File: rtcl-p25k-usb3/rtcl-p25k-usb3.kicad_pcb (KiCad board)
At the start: 2 copper layers, 83 parts, among them J5 JTAG, U1 FT601Q, U12 TPS22917DBV, U2 TPD4E05U06DQA, U3 USBLC6-2P6

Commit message: WIP
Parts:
- added R51: 0, Resistor_SMD:R_0402_1005Metric, F.Cu at (159.3, 102.0)
- added R52: 0, Resistor_SMD:R_0402_1005Metric, F.Cu at (159.3, 103.0)
- added RN1: R_Pack04, Resistor_SMD:R_Array_Convex_4x0603, F.Cu at (156.6, 103.6)
- added Y1: 30MHz, Resistor_SMD:R_Array_Convex_4x0402, F.Cu at (169.9, 103.7)
- L1: footprint Inductor_SMD:L_0603_1608Metric -> Resistor_SMD:R_0402_1005Metric
- R1, R10, R11, R12, R13, R14, R15, R16, R17, R18, R19, R2, R20, R21, R22, R23, R24, R25, R26, R27, R28, R29, R3, R30, R31, R32, R33, R34, R35, R36, R37, R38, R39, R4, R40, R41, R42, R43, R44, R45, R46, R47, R48, R49, R5, R50, R51, R52, R53, R54, R55, R56, R57, R58, R6, R7, R8, R9: footprint Resistor_SMD:R_0603_1608Metric -> Resistor_SMD:R_0402_1005Metric
- moved R51 24.2 mm to (159.3, 104.0)
- moved R52 23.8 mm to (159.3, 105.0)
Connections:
- R39 pad 1: /FT601_BE0 -> unconnected-(R39-Pad1)
- R40 pad 1: /FT601_BE1 -> unconnected-(R40-Pad1)
- R41 pad 1: /FT601_BE2 -> unconnected-(R41-Pad1)
- R42 pad 1: /FT601_BE3 -> unconnected-(R42-Pad1)

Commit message: WIP
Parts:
- added J3: BTB-DF40C-60DS-0.4V(51), rtcl-p25k-usb3:CONN_DF40C-60DS_HIR, F.Cu at (150.0, 107.0)
- added J4: BTB-DF40C-60DS-0.4V(51), rtcl-p25k-usb3:CONN_DF40C-60DS_HIR, F.Cu at (150.0, 93.0)
- moved C13 100.7 mm to (46.0, 148.6)
- moved C14 100.7 mm to (46.0, 151.1)
- moved C5 100.7 mm to (46.0, 141.1)
- moved C69 100.7 mm to (74.9, 155.8)
- moved D1 100.7 mm to (45.6, 171.1)
- moved J5 100.7 mm to (70.4, 142.1)
- moved L1 100.7 mm to (46.0, 158.7)
- moved R12 100.7 mm to (50.0, 158.7)
- moved R15 100.7 mm to (50.0, 166.2)
- moved R17 100.7 mm to (54.0, 141.1)
- moved R20 100.7 mm to (54.0, 148.6)
- moved R21 100.7 mm to (54.0, 151.1)
- moved R24 100.7 mm to (54.0, 158.7)
- moved R27 100.7 mm to (54.0, 166.2)
- moved R29 100.7 mm to (58.1, 141.1)
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- renumbered Y1 to X1

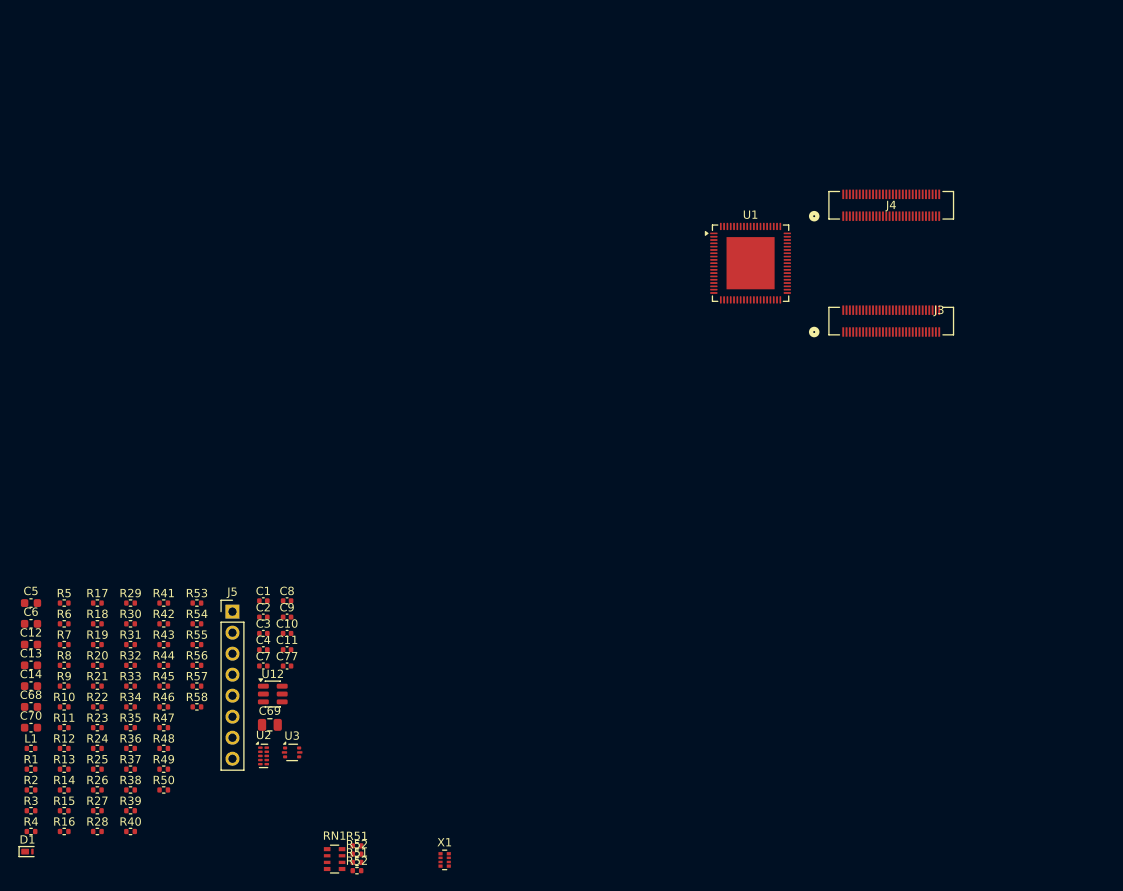
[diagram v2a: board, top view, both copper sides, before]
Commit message: Add new footprints for RES_YC104_YAG and RES_YC164_3P2X1P6_YAG
- Created footprint for RES_YC104_YAG with detailed properties and pads.
- Created footprint for RES_YC164_3P2X1P6_YAG with comprehensive design elements and specifications.
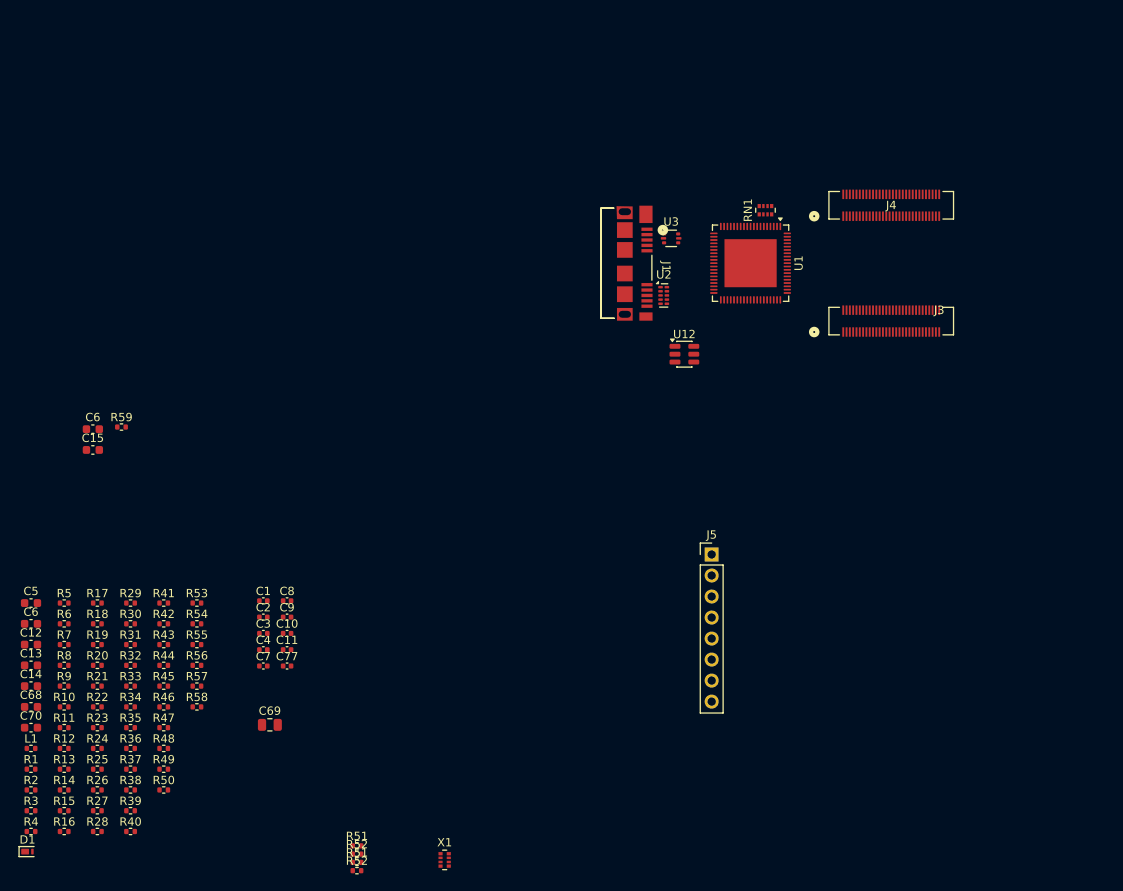
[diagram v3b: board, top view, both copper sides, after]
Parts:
- added C15: 0.1uF, Capacitor_SMD:C_0603_1608Metric, F.Cu at (53.5, 122.6)
- added C6: 4.7uF, Capacitor_SMD:C_0603_1608Metric, F.Cu at (53.5, 120.1)
- added J1: ZX360D-B-10P(30), rtcl-p25k-usb3:CONN10_ZX360D-B-10P30_HIR, F.Cu at (118.0, 100.0)
- added R59: 1M, Resistor_SMD:R_0402_1005Metric, F.Cu at (57.0, 119.8)
- RN1: footprint Resistor_SMD:R_Array_Convex_4x0603 -> Resistor_SMD:R_Array_Convex_4x0402
- moved RN1 94.1 mm to (134.8, 93.6), turned to 90 degrees
- moved U3 77.2 mm to (123.4, 97.0)
- moved U2 73.7 mm to (122.5, 103.9)
- moved U12 64.5 mm to (125.0, 111.0)
- moved J5 58.3 mm to (128.3, 135.2)
- turned U1 to -90 degrees
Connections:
- C10 pad 2: +5V -> VBUS
- RN1 pad 1: unconnected-(RN1-R1.1-Pad1) -> /FT601_BE3
- RN1 pad 2: unconnected-(RN1-R2.1-Pad2) -> /FT601_BE2
- RN1 pad 3: unconnected-(RN1-R3.1-Pad3) -> /FT601_BE1
- RN1 pad 4: unconnected-(RN1-R4.1-Pad4) -> /FT601_BE0
- RN1 pad 5: /FT601_BE0 -> unconnected-(RN1-R4.2-Pad5)
- RN1 pad 6: /FT601_BE1 -> unconnected-(RN1-R3.2-Pad6)
- RN1 pad 7: /FT601_BE2 -> unconnected-(RN1-R2.2-Pad7)
- RN1 pad 8: /FT601_BE3 -> unconnected-(RN1-R1.2-Pad8)
- U1 pad 37: +5V -> VBUS
- U2 pad 1: /USB_SSRXP -> /USB_SSTXM
- U2 pad 2: /USB_SSRXM -> /USB_SSTXP
- U2 pad 4: /USB_SSTXP -> /USB_SSRXM
- U2 pad 5: /USB_SSTXM -> /USB_SSRXP
- U3 pad 5: +5V -> VBUS

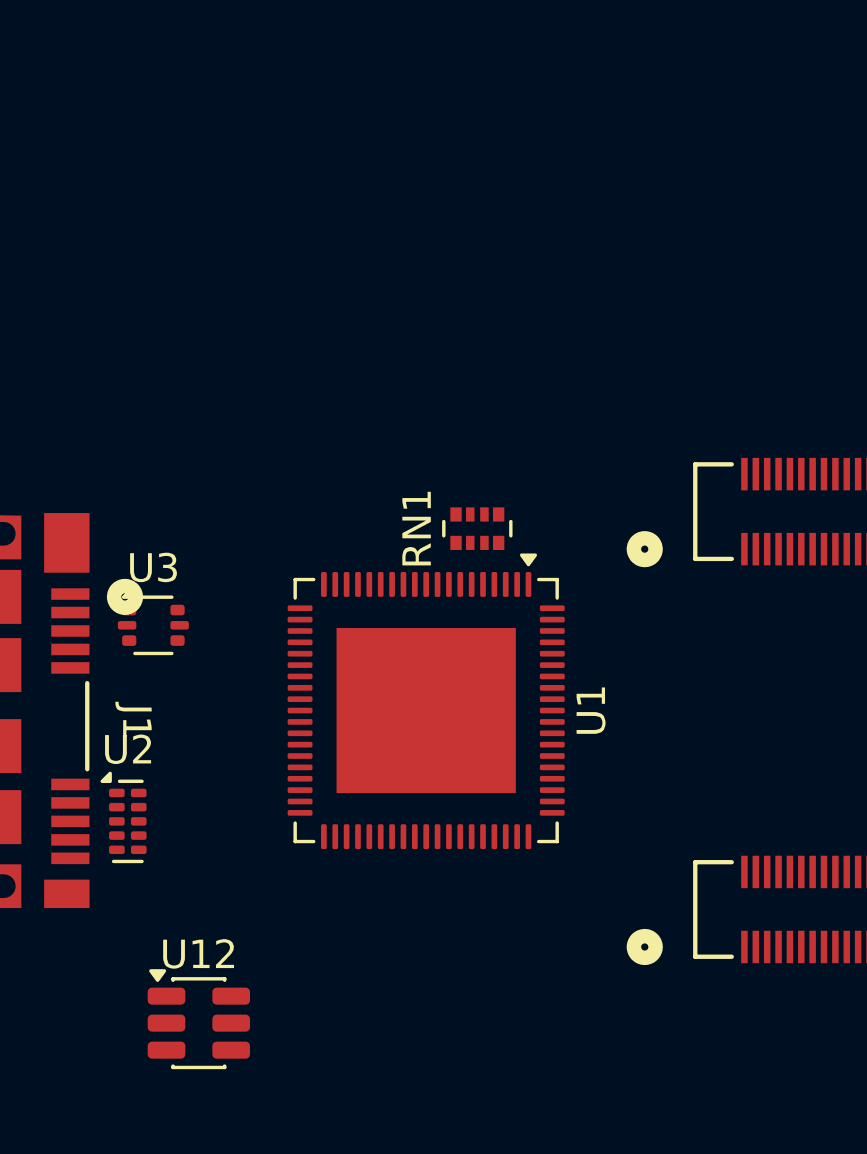
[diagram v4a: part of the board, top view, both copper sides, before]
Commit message: Add FT601Q symbol to KiCad library
- Created a new symbol for the FT601Q USB 3.0 FIFO interface IC.
- Included properties such as Reference, Value, Footprint, Datasheet, and Description.
- Defined 77 pins with appropriate names, types, and attributes.
- Ensured compatibility with KiCad version 10.0 and included necessary font settings.
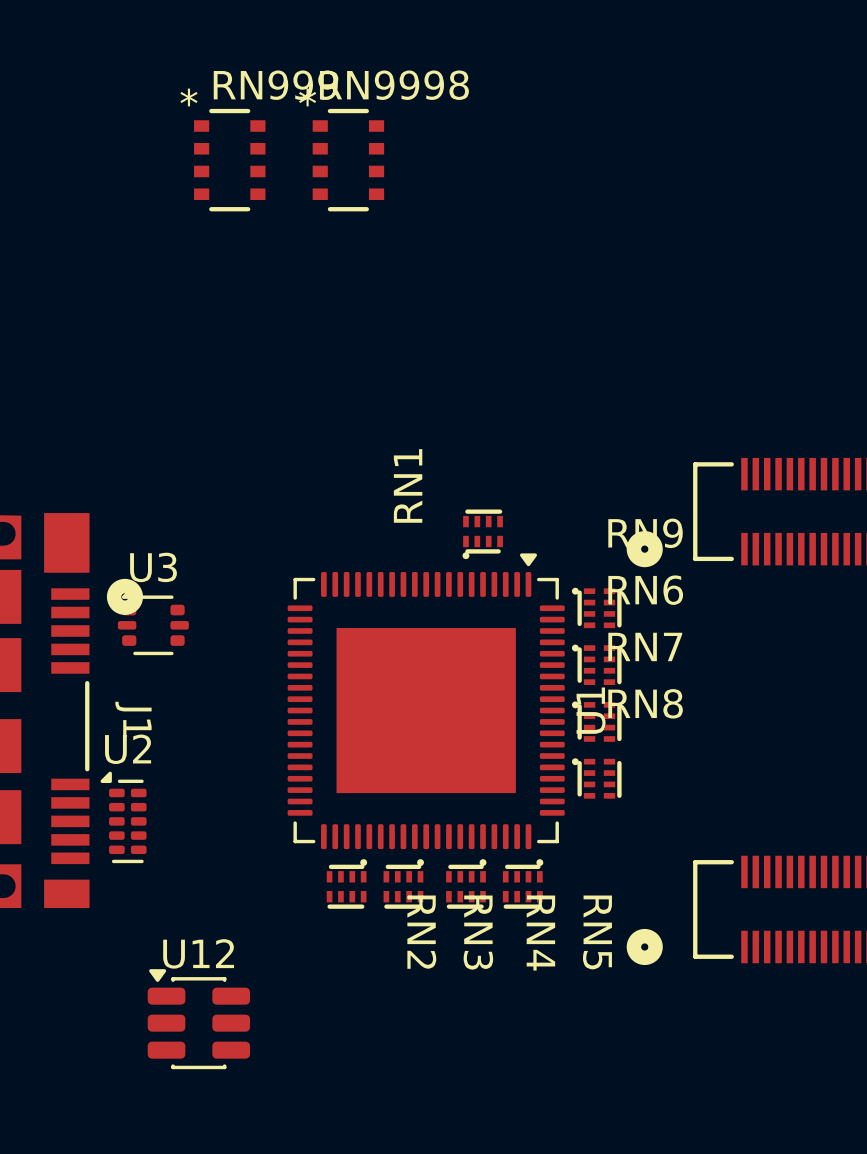
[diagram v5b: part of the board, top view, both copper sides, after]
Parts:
- added RN2: YC104-JR-0722RL, rtcl-p25k-usb3:RES_YC104_YAG, F.Cu at (130.2, 106.2)
- added RN3: YC104-JR-0722RL, rtcl-p25k-usb3:RES_YC104_YAG, F.Cu at (132.2, 106.2)
- added RN4: YC104-JR-0722RL, rtcl-p25k-usb3:RES_YC104_YAG, F.Cu at (134.4, 106.2)
- added RN5: YC104-JR-0722RL, rtcl-p25k-usb3:RES_YC104_YAG, F.Cu at (136.4, 106.2)
- added RN6: YC104-JR-0722RL, rtcl-p25k-usb3:RES_YC104_YAG, F.Cu at (139.1, 98.4)
- added RN7: YC104-JR-0722RL, rtcl-p25k-usb3:RES_YC104_YAG, F.Cu at (139.1, 100.4)
- added RN8: YC104-JR-0722RL, rtcl-p25k-usb3:RES_YC104_YAG, F.Cu at (139.1, 102.4)
- added RN9: YC104-JR-0722RL, rtcl-p25k-usb3:RES_YC104_YAG, F.Cu at (139.1, 96.4)
- added RN999: YC164-JR-0722RL, rtcl-p25k-usb3:RES_YC164_3P2X1P6_YAG, F.Cu at (126.1, 80.6)
- added RN9998: YC124-JR-1322RL, rtcl-p25k-usb3:RES_YC164_3P2X1P6_YAG, F.Cu at (130.3, 80.6)
- RN1: value R_Pack04 -> YC104-JR-0722RL; footprint Resistor_SMD:R_Array_Convex_4x0402 -> rtcl-p25k-usb3:RES_YC104_YAG
- moved RN1 0.22 mm to (135.0, 93.7)
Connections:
- R43 pad 1: /FT601_CLK -> /FT601_SIWU
- U1 pad 10: /FT601_CLK -> /FT601_SIWU

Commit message: WIP
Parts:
- removed the C6 at (46.0, 143.6)
- removed D1: PTVS5V0Z1USKP, Diode_SMD:Nexperia_DSN1608-2_1.6x0.8mm
- removed L1: BLM18PG221SN1D, Resistor_SMD:R_0402_1005Metric
- removed R10, R11, R12, R13, R14, R15, R16, R17, R18, R19, R20, R21, R22, R23, R24, R25, R26, R27, R28, R29, R30, R31, R32, R33, R34, R35, R36, R37, R38, R39, R4, R40, R41, R42, R44, R45, R46, R47, R48, R5, R6, R7, R8, R9: 22, Resistor_SMD:R_0402_1005Metric
- removed the R51 at (85.4, 170.4)
- removed the R52 at (85.4, 171.4)
- removed R55: 0, Resistor_SMD:R_0402_1005Metric
- removed U1: FT601Q, Package_DFN_QFN:QFN-76-1EP_9x9mm_P0.4mm_EP5.81x6.31mm
- added RN10: YC104-JR-0722RL, rtcl-p25k-usb3:RES_YC104_YAG, F.Cu at (126.4, 93.7)
- added RN11: YC104-JR-0722RL, rtcl-p25k-usb3:RES_YC104_YAG, F.Cu at (124.4, 93.7)
- added U4: FT601Q, Package_DFN_QFN:QFN-76-1EP_9x9mm_P0.4mm_EP5.81x6.31mm, F.Cu at (126.0, 100.0)
- moved R43 74.8 mm to (125.6, 106.6)
- moved RN6 6.75 mm to (132.3, 98.4)
- moved RN7 6.75 mm to (132.3, 100.4)
- moved RN8 6.75 mm to (132.3, 102.4)
- moved RN9 6.75 mm to (132.3, 96.4)
- moved RN1 6.60 mm to (128.4, 93.7)
- moved J1 6.50 mm to (111.5, 100.0)
- moved RN4 6.50 mm to (127.9, 106.2)
- moved RN5 6.50 mm to (129.9, 106.2)
- moved U12 6.50 mm to (118.5, 111.0)
- moved U2 6.50 mm to (116.0, 103.9)
- moved U3 6.50 mm to (116.9, 97.0)
- moved RN2 6.50 mm to (123.7, 106.2)
- moved RN3 6.50 mm to (125.7, 106.2)
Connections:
- R2 pad 2: Net-(U1-~{WAKEUP}) -> /FT601_WAKEUP
- R43 pad 1: /FT601_SIWU -> /FT601_CLK
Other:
- board outline added: 56 x 28.3 mm

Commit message: WIP
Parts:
- moved J5 50.9 mm to (136.9, 85.0), turned to 90 degrees
- moved U12 7.43 mm to (111.5, 113.5)
- moved J1 6.12 mm to (117.6, 100.0)
- moved U2 6.12 mm to (122.1, 103.9)
- moved U3 5.80 mm to (122.7, 97.0)
- moved RN1 5.00 mm to (133.4, 93.7)
- moved RN10 5.00 mm to (131.4, 93.7)
- moved RN11 5.00 mm to (129.4, 93.7)
- moved RN4 5.00 mm to (132.9, 106.2)
- moved RN5 5.00 mm to (134.9, 106.2)
- moved RN6 5.00 mm to (137.3, 98.4)
- moved RN7 5.00 mm to (137.3, 100.4)
- moved RN8 5.00 mm to (137.3, 102.4)
- moved RN9 5.00 mm to (137.3, 96.4)
- moved U4 5.00 mm to (131.0, 100.0)
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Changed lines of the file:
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@@
 	(footprint "rtcl-p25k-usb3:RES_YC104_YAG"
 		(layer "F.Cu")
-		(at 126.4 93.7 90)
+		(at 131.4 93.745 90)
 		(tags "YC164-JR-0722RL ")
 		(property "Reference" "RN10"
@@
 	(footprint "Package_TO_SOT_SMD:SOT-666"
 		(layer "F.Cu")
-		(at 116.9 97)
+		(at 122.7 97)
 		(descr "SOT666")
 		(tags "SOT-666")
@@
 	(footprint "rtcl-p25k-usb3:RES_YC104_YAG"
 		(layer "F.Cu")
-		(at 132.35 96.4)
+		(at 137.35 96.445)
 		(tags "YC164-JR-0722RL ")
 		(property "Reference" "RN9"
@@
 	(footprint "Resistor_SMD:R_0402_1005Metric"
 		(layer "F.Cu")
-		(at 125.645 106.605)
+		(at 129.11 110.2)
 		(descr "Resistor SMD 0402 (1005 Metric), square (rectangular) end terminal, IPC-7351 nominal, (Body size source: IPC-SM-782 page 72, https://www.pcb-3d.com/wordpress/wp-content/uploads/ipc-sm-782a_amendment_1_and_2.pdf)")
 		(tags "resistor")
@@
 	(footprint "rtcl-p25k-usb3:RES_YC104_YAG"
 		(layer "F.Cu")
-		(at 128.4 93.7 90)
+		(at 133.4 93.745 90)
 		(tags "YC164-JR-0722RL ")
 		(property "Reference" "RN1"
@@
 	(footprint "Connector_PinHeader_2.54mm:PinHeader_1x08_P2.54mm_Vertical"
 		(layer "F.Cu")
-		(at 128.3 135.21)
+		(at 136.88 85 90)
 		(descr "Through hole straight pin header, 1x08, 2.54mm pitch, single row")
 		(tags "Through hole pin header THT 1x08 2.54mm single row")
 		(property "Reference" "J5"
-			(at 0 -2.38 0)
+			(at 0 -2.38 90)
 			(layer "F.SilkS")
 			(effects
@@
 		)
 		(property "Value" "JTAG"
-			(at 0 20.16 0)
+			(at 0 20.16 90)
 			(layer "F.Fab")
 			(effects
@@
 		)
 		(property "Datasheet" ""
-			(at 0 0 0)
+			(at 0 0 90)
 			(layer "F.Fab")
 			(hide yes)
@@
 		)
 		(property "Description" "Generic connector, single row, 01x06, script generated (kicad-library-utils/schlib/autogen/connector/)"
-			(at 0 0 0)
+			(at 0 0 90)
 			(layer "F.Fab")
 			(hide yes)
@@
 		)
 		(property "KiLib_Generator" "connector/pin_header_socket"
-			(at 0 0 0)
+			(at 0 0 90)
 			(layer "F.SilkS")
 			(hide yes)
@@
 		)
 		(fp_line
-			(start -1.38 1.27)
-			(end -1.38 19.16)
+			(start 1.38 1.27)
+			(end 1.38 19.16)
 			(stroke
 				(width 0.12)
@@
 		)
 		(fp_line
-			(start -1.38 19.16)
-			(end 1.38 19.16)
+			(start -1.38 1.27)
+			(end -1.38 19.16)
 			(stroke
 				(width 0.12)
@@
 		)
 		(fp_line
-			(start 1.38 1.27)
+			(start -1.38 19.16)
 			(end 1.38 19.16)
 			(stroke
@@
 		)
 		(fp_line
-			(start -1.27 -0.635)
-			(end -0.635 -1.27)
+			(start 1.27 -1.27)
+			(end 1.27 19.05)
 			(stroke
 				(width 0.1)
@@
 		)
 		(fp_line
-			(start -1.27 19.05)
-			(end -1.27 -0.635)
+			(start -0.635 -1.27)
+			(end 1.27 -1.27)
 			(stroke
 				(width 0.1)
@@
 		)
 		(fp_line
-			(start -0.635 -1.27)
-			(end 1.27 -1.27)
+			(start -1.27 -0.635)
+			(end -0.635 -1.27)
 			(stroke
 				(width 0.1)
@@
 		)
 		(fp_line
-			(start 1.27 -1.27)
-			(end 1.27 19.05)
+			(start 1.27 19.05)
+			(end -1.27 19.05)
 			(stroke
 				(width 0.1)
@@
 		)
 		(fp_line
-			(start 1.27 19.05)
-			(end -1.27 19.05)
+			(start -1.27 19.05)
+			(end -1.27 -0.635)
 			(stroke
 				(width 0.1)
@@
 		)
 		(fp_text user "${REFERENCE}"
-			(at 0 8.89 90)
+			(at 0 8.89 0)
 			(layer "F.Fab")
 			(effects
@@
 		)
 		(pad "1" thru_hole rect
-			(at 0 0)
+			(at 0 0 90)
 			(size 1.7 1.7)
 			(drill 1)
@@
 		)
 		(pad "2" thru_hole circle
-			(at 0 2.54)
+			(at 0 2.54 90)
 			(size 1.7 1.7)
 			(drill 1)
@@
 		)
 		(pad "3" thru_hole circle
-			(at 0 5.08)
+			(at 0 5.08 90)
 			(size 1.7 1.7)
 			(drill 1)
@@
 		)
 		(pad "4" thru_hole circle
-			(at 0 7.62)
+			(at 0 7.62 90)
 			(size 1.7 1.7)
 			(drill 1)
@@
 		)
 		(pad "5" thru_hole circle
-			(at 0 10.16)
+			(at 0 10.16 90)
 			(size 1.7 1.7)
 			(drill 1)
@@
 		)
 		(pad "6" thru_hole circle
-			(at 0 12.7)
+			(at 0 12.7 90)
 			(size 1.7 1.7)
 			(drill 1)
@@
 		)
 		(pad "7" thru_hole circle
-			(at 0 15.24)
+			(at 0 15.24 90)
 			(size 1.7 1.7)
 			(drill 1)
@@
 		)
 		(pad "8" thru_hole circle
-			(at 0 17.78)
+			(at 0 17.78 90)
 			(size 1.7 1.7)
 			(drill 1)
@@
 		(tags "DF40C-60DS-0.4V51 ")
 		(property "Reference" "J3"
-			(at 5.799999 -1.32 0)
+			(at -0.000001 -3 0)
 			(unlocked yes)
 			(layer "F.SilkS")
@@
 	(footprint "Package_SON:USON-10_2.5x1.0mm_P0.5mm"
 		(layer "F.Cu")
-		(at 116 103.9)
+		(at 122.1208 103.9)
 		(descr "USON-10 2.5x1.0mm_ Pitch 0.5mm http://www.ti.com/lit/ds/symlink/tpd4e02b04.pdf")
 		(tags "USON-10 2.5x1.0mm Pitch 0.5mm")
@@
 	(footprint "rtcl-p25k-usb3:RES_YC104_YAG"
 		(layer "F.Cu")
-		(at 127.9 106.2 -90)
+		(at 132.9 106.245 -90)
 		(tags "YC164-JR-0722RL ")
 		(property "Reference" "RN4"
@@
 	(footprint "rtcl-p25k-usb3:RES_YC104_YAG"
 		(layer "F.Cu")
-		(at 132.35 102.4)
+		(at 137.35 102.445)
 		(tags "YC164-JR-0722RL ")
 		(property "Reference" "RN8"
@@
 	(footprint "rtcl-p25k-usb3:RES_YC104_YAG"
 		(layer "F.Cu")
-		(at 129.9 106.2 -90)
+		(at 134.9 106.245 -90)
 		(tags "YC164-JR-0722RL ")
 		(property "Reference" "RN5"
@@
 	(footprint "rtcl-p25k-usb3:RES_YC104_YAG"
 		(layer "F.Cu")
-		(at 123.7 106.2 -90)
+		(at 128.7 106.245 -90)
 		(tags "YC164-JR-0722RL ")
 		(property "Reference" "RN2"
@@
 	(footprint "Package_TO_SOT_SMD:SOT-23-6"
 		(layer "F.Cu")
-		(at 118.5 111)
+		(at 111.5 113.5)
 		(descr "SOT, 6 Pin (JEDEC MO-178 Var AB https://www.jedec.org/document_search?search_api_views_fulltext=MO-178)")
 		(tags "SOT TO_SOT_SMD")
@@
 	(footprint "rtcl-p25k-usb3:CONN10_ZX360D-B-10P30_HIR"
 		(layer "F.Cu")
-		(at 111.5 100 -90)
+		(at 117.6208 100 -90)
 		(tags "ZX360D-B-10P30 ")
 		(property "Reference" "J1"
@@
 	(footprint "rtcl-p25k-usb3:RES_YC104_YAG"
 		(layer "F.Cu")
-		(at 125.7 106.2 -90)
+		(at 130.7 106.245 -90)
 		(tags "YC164-JR-0722RL ")
 		(property "Reference" "RN3"
@@
 	(footprint "rtcl-p25k-usb3:RES_YC104_YAG"
 		(layer "F.Cu")
-		(at 124.4 93.7 90)
+		(at 129.4 93.745 90)
 		(tags "YC164-JR-0722RL ")
 		(property "Reference" "RN11"
@@
 		(tags "DF40C-60DS-0.4V51 ")
 		(property "Reference" "J4"
-			(at -0.000001 0 0)
+			(at -0.000001 3 0)
 			(unlocked yes)
 			(layer "F.SilkS")
@@
 	(footprint "rtcl-p25k-usb3:RES_YC104_YAG"
 		(layer "F.Cu")
-		(at 132.35 100.4)
+		(at 137.35 100.445)
 		(tags "YC164-JR-0722RL ")
 		(property "Reference" "RN7"
@@
 	(footprint "rtcl-p25k-usb3:RES_YC104_YAG"
 		(layer "F.Cu")
-		(at 132.35 98.4)
+		(at 137.35 98.445)
 		(tags "YC164-JR-0722RL ")
 		(property "Reference" "RN6"
@@
 	(footprint "Package_DFN_QFN:QFN-76-1EP_9x9mm_P0.4mm_EP5.81x6.31mm"
 		(layer "F.Cu")
-		(at 126 99.955 -90)
+		(at 131 100 -90)
 		(descr "QFN, 76 Pin (https://ftdichip.com/wp-content/uploads/2020/07/DS_FT600Q-FT601Q-IC-Datasheet.pdf#page=27)")
 		(tags "QFN NoLead")
@@
 	)
 	(gr_line
-		(start 93.25 100)
-		(end 214.25 100)
+		(start 98.25 100.045)
+		(end 219.25 100.045)
 		(stroke
 			(width 0.1)
@@
 	)
 	(gr_line
-		(start 122 93)
-		(end 174 93)
+		(start 127 93.045)
+		(end 179 93.045)
 		(stroke
 			(width 0.1)
@@
 	)
 	(gr_line
-		(start 170 107)
-		(end 124 107)
+		(start 175 107.045)
+		(end 129 107.045)
 		(stroke
 			(width 0.1)

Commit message: WIP
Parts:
- added J2: 0525592253, rtcl-p25k-usb3:CON_525592253_MOL, F.Cu at (167.0, 100.0)
- moved J5 3.56 mm to (140.3, 86.0)
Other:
- board size 56 x 28.3 mm -> 60 x 32.3 mm
